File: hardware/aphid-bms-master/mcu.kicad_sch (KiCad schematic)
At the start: 7 parts, among them J6 DEBUG, U1 STM32G491CCTx, Y1 8 MHz

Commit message: Assigned some footprints
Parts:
- C2, C3: footprint (none) -> Capacitor_SMD:C_0805_2012Metric
- J6: footprint (none) -> Connector_PinHeader_1.27mm:PinHeader_2x07_P1.27mm_Vertical_SMD
- JP1: footprint (none) -> Jumper:SolderJumper-2_P1.3mm_Open_TrianglePad1.0x1.5mm
- R3: footprint (none) -> Resistor_SMD:R_0805_2012Metric
- Y1: footprint (none) -> aphid:ABM3-x.xxxMHZ-D2Y-T
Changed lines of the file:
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@@
 			)
 		)
-		(property "Footprint" ""
+		(property "Footprint" "aphid:ABM3-x.xxxMHZ-D2Y-T"
 			(at 54.61 81.28 0)
 			(effects
@@
 			)
 		)
-		(property "Footprint" ""
+		(property "Footprint" "Capacitor_SMD:C_0805_2012Metric"
 			(at 49.2252 91.44 0)
 			(effects
@@
 			)
 		)
-		(property "Footprint" ""
+		(property "Footprint" "Connector_PinHeader_1.27mm:PinHeader_2x07_P1.27mm_Vertical_SMD"
 			(at 45.72 167.64 0)
 			(effects
@@
 			)
 		)
-		(property "Footprint" ""
+		(property "Footprint" "Capacitor_SMD:C_0805_2012Metric"
 			(at 59.9948 91.44 0)
 			(effects
@@
 			)
 		)
-		(property "Footprint" ""
+		(property "Footprint" "Jumper:SolderJumper-2_P1.3mm_Open_TrianglePad1.0x1.5mm"
 			(at 41.91 68.58 0)
 			(effects
@@
 			)
 		)
-		(property "Footprint" ""
+		(property "Footprint" "Resistor_SMD:R_0805_2012Metric"
 			(at 35.052 109.22 90)
 			(effects

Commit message: Worked on BMS master
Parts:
- removed JP1: PRIMARY, Jumper:SolderJumper-2_P1.3mm_Open_TrianglePad1.0x1.5mm, symbol Jumper:SolderJumper_2_Open
- added C16: 100nF, Capacitor_SMD:C_0805_2012Metric, symbol Device:C
- added C17: 1uF, Capacitor_SMD:C_0805_2012Metric, symbol Device:C
- added C18, C19, C20, C21: 100nF, Capacitor_SMD:C_0603_1608Metric, symbol Device:C
- added D5: STATUS, LED_SMD:LED_0805_2012Metric, symbol Device:LED
- added FB1: 600 ohm, Inductor_SMD:L_0805_2012Metric, symbol Device:FerriteBead
- added JP3: BOOT, Jumper:SolderJumper-3_P1.3mm_Bridged12_RoundedPad1.0x1.5mm_NumberLabels, symbol Jumper:SolderJumper_3_Bridged12
- added R12: R, Resistor_SMD:R_0805_2012Metric, symbol Device:R
- C2, C3: value C -> 22pF
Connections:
- net +3.3V: now also J6.3 (VCC), R3.1, U1.1 (VBAT), U1.24 (VDD), U1.36 (VDD), U1.48 (VDD), C19.1, C20.1, C21.1, FB1.1, JP3.3 (B)
- net BOOT1: now also JP3.2 (C)
- net DBG_RX: now also J6.13 (VCP_RX)
- net DBG_TX: now also J6.14 (VCP_TX)
- net DRIVER_FAULT: now also U1.12 (PA4)
- net ENABLE_DRIVER: now also U1.10 (PA2)
- net GND: now also C2.2, C3.2, J6.11 (GNDDetect), J6.5 (GND), J6.7 (GND), U1.19 (VSSA), U1.23 (VSS), U1.35 (VSS), U1.47 (VSS), C16.2, C17.2, C18.2, C19.2, C20.2, C21.2, D5.1 (K), JP3.1 (A)
- net LED: now also R12.1
- net NRST: now also J6.12 (~{RST}), R3.2, C16.1
- net OSC_IN: now also C2.1, Y1.1
- net OSC_OUT: now also C3.1, Y1.2
- net PRIMARY: now also U1.17 (PB1); no longer U1.11 (PA3)
- net RESET_DRIVER: now also U1.11 (PA3)
- net SWCLK: now also J6.6 (JCLK/SWCLK)
- net SWDIO: now also J6.4 (JTMS/SWDIO)
- net SWO: now also J6.8 (JTDO/SWO)
- net VDDA: now reaches U1.20 (VREF+)
- net VDDA: now also U1.21 (VDDA), C17.1, C18.1, FB1.2
- new net: D5.2 (A), R12.2
- no-connect marks 0 -> 14
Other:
- note added: "BOOT0 = Low -> Boot from FLASH BOOT0 = High -> Boot from System memory (ROM bootloader)"
- note added: "CL = 18 pF Cs = ~7 pF CL1 = CL2 = 2 * (Cl - Cs) CL1 = CL2 = 22 pF"
- note added: "Filter Analog supply some extra from noise"
- note added: "One 100 nF decoupling per VDD-pin. Bulk decoupling on Power-sheet"
- note added: "Pull up and filter on NRST to reduce risk of spurious resets"
- company: (none) -> https://aphid-ev.se
- title: (none) -> Aphid BMS Master
- moved on the sheet: C2, C3, R3, Y1

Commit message: Worked on BMS master layout
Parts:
- C2, C3: footprint Capacitor_SMD:C_0805_2012Metric -> Capacitor_SMD:C_0603_1608Metric
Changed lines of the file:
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@@
 			)
 		)
-		(property "Footprint" "Capacitor_SMD:C_0805_2012Metric"
+		(property "Footprint" "Capacitor_SMD:C_0603_1608Metric"
 			(at 33.9852 78.74 0)
 			(effects
@@
 			)
 		)
-		(property "Footprint" "Capacitor_SMD:C_0805_2012Metric"
+		(property "Footprint" "Capacitor_SMD:C_0603_1608Metric"
 			(at 44.7548 78.74 0)
 			(effects

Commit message: Worked on BMS master layout
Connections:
- net CAN1_RX: now also U1.26 (PB12); no longer U1.33 (PA11)
- net CAN1_STB: now also U1.28 (PB14); no longer U1.32 (PA10)
- net CAN1_TX: now also U1.27 (PB13); no longer U1.34 (PA12)
- net CAN2_RX: now also U1.33 (PA11); no longer U1.26 (PB12)
- net CAN2_STB: now also U1.32 (PA10); no longer U1.25 (PB11)
- net CAN2_TX: now also U1.34 (PA12); no longer U1.27 (PB13)
- net LED: now also U1.3 (PC14); no longer U1.16 (PB0)
- net PRIMARY: now also U1.30 (PA8); no longer U1.17 (PB1)
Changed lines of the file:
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@@
 		(color 0 0 0 0)
 	)
-	(no_connect
-		(at 121.92 123.19)
+	(junction
+		(at 154.94 80.01)
+		(diameter 0)
+		(color 0 0 0 0)
+	)
+	(no_connect
+		(at 121.92 115.57)
 	)
 	(no_connect
@@
 	)
 	(no_connect
+		(at 121.92 90.17)
+	)
+	(no_connect
 		(at 121.92 82.55)
 	)
@@
 	)
 	(no_connect
-		(at 121.92 80.01)
-	)
-	(no_connect
-		(at 154.94 80.01)
+		(at 121.92 87.63)
 	)
 	(wire
@@
 	(wire
 		(pts
-			(xy 109.22 115.57) (xy 121.92 115.57)
+			(xy 110.49 123.19) (xy 121.92 123.19)
 		)
 		(stroke
@@
 	(wire
 		(pts
-			(xy 109.22 90.17) (xy 121.92 90.17)
+			(xy 166.37 80.01) (xy 154.94 80.01)
 		)
 		(stroke
@@
 	(wire
 		(pts
-			(xy 109.22 120.65) (xy 121.92 120.65)
+			(xy 110.49 120.65) (xy 121.92 120.65)
 		)
 		(stroke
@@
 	(wire
 		(pts
-			(xy 109.22 118.11) (xy 121.92 118.11)
+			(xy 110.49 118.11) (xy 121.92 118.11)
 		)
 		(stroke
@@
 	(wire
 		(pts
-			(xy 109.22 125.73) (xy 121.92 125.73)
+			(xy 110.49 125.73) (xy 121.92 125.73)
 		)
 		(stroke
@@
 	(wire
 		(pts
-			(xy 113.03 87.63) (xy 121.92 87.63)
+			(xy 113.03 80.01) (xy 121.92 80.01)
 		)
 		(stroke
@@
 		(pts
 			(xy 250.19 85.09) (xy 250.19 87.63)
+		)
+		(stroke
+			(width 0)
+			(type default)
+		)
+	)
+	(wire
+		(pts
+			(xy 153.67 80.01) (xy 154.94 80.01)
 		)
 		(stroke
@@
 	)
 	(label "LED"
-		(at 113.03 87.63 0)
+		(at 113.03 80.01 0)
 		(fields_autoplaced yes)
 		(effects
@@
 	(hierarchical_label "CAN2_RX"
 		(shape input)
-		(at 109.22 118.11 180)
-		(fields_autoplaced yes)
-		(effects
-			(font
-				(size 1.27 1.27)
-			)
-			(justify right)
+		(at 166.37 87.63 0)
+		(fields_autoplaced yes)
+		(effects
+			(font
+				(size 1.27 1.27)
+			)
+			(justify left)
 		)
 	)
 	(hierarchical_label "CAN1_STB"
 		(shape output)
-		(at 166.37 85.09 0)
-		(fields_autoplaced yes)
-		(effects
-			(font
-				(size 1.27 1.27)
-			)
-			(justify left)
+		(at 110.49 123.19 180)
+		(fields_autoplaced yes)
+		(effects
+			(font
+				(size 1.27 1.27)
+			)
+			(justify right)
 		)
 	)
 	(hierarchical_label "CAN2_TX"
 		(shape output)
-		(at 109.22 120.65 180)
-		(fields_autoplaced yes)
-		(effects
-			(font
-				(size 1.27 1.27)
-			)
-			(justify right)
+		(at 166.37 90.17 0)
+		(fields_autoplaced yes)
+		(effects
+			(font
+				(size 1.27 1.27)
+			)
+			(justify left)
 		)
 	)
@@
 	(hierarchical_label "PRIMARY"
 		(shape input)
-		(at 109.22 90.17 180)
-		(fields_autoplaced yes)
-		(effects
-			(font
-				(size 1.27 1.27)
-			)
-			(justify right)
+		(at 166.37 80.01 0)
+		(fields_autoplaced yes)
+		(effects
+			(font
+				(size 1.27 1.27)
+			)
+			(justify left)
 		)
 	)
@@
 	(hierarchical_label "CAN1_RX"
 		(shape input)
-		(at 166.37 87.63 0)
-		(fields_autoplaced yes)
-		(effects
-			(font
-				(size 1.27 1.27)
-			)
-			(justify left)
+		(at 110.49 118.11 180)
+		(fields_autoplaced yes)
+		(effects
+			(font
+				(size 1.27 1.27)
+			)
+			(justify right)
 		)
 	)
@@
 	(hierarchical_label "CAN2_STB"
 		(shape output)
-		(at 109.22 115.57 180)
-		(fields_autoplaced yes)
-		(effects
-			(font
-				(size 1.27 1.27)
-			)
-			(justify right)
+		(at 166.37 85.09 0)
+		(fields_autoplaced yes)
+		(effects
+			(font
+				(size 1.27 1.27)
+			)
+			(justify left)
 		)
 	)
 	(hierarchical_label "ENABLE_SLAVES"
 		(shape output)
-		(at 109.22 125.73 180)
+		(at 110.49 125.73 180)
 		(fields_autoplaced yes)
 		(effects
@@
 	(hierarchical_label "CAN1_TX"
 		(shape output)
-		(at 166.37 90.17 0)
-		(fields_autoplaced yes)
-		(effects
-			(font
-				(size 1.27 1.27)
-			)
-			(justify left)
-		)
-	)
+		(at 110.49 120.65 180)
+		(fields_autoplaced yes)
+		(effects
+			(font
+				(size 1.27 1.27)
+			)
+			(justify right)
+		)
+	)

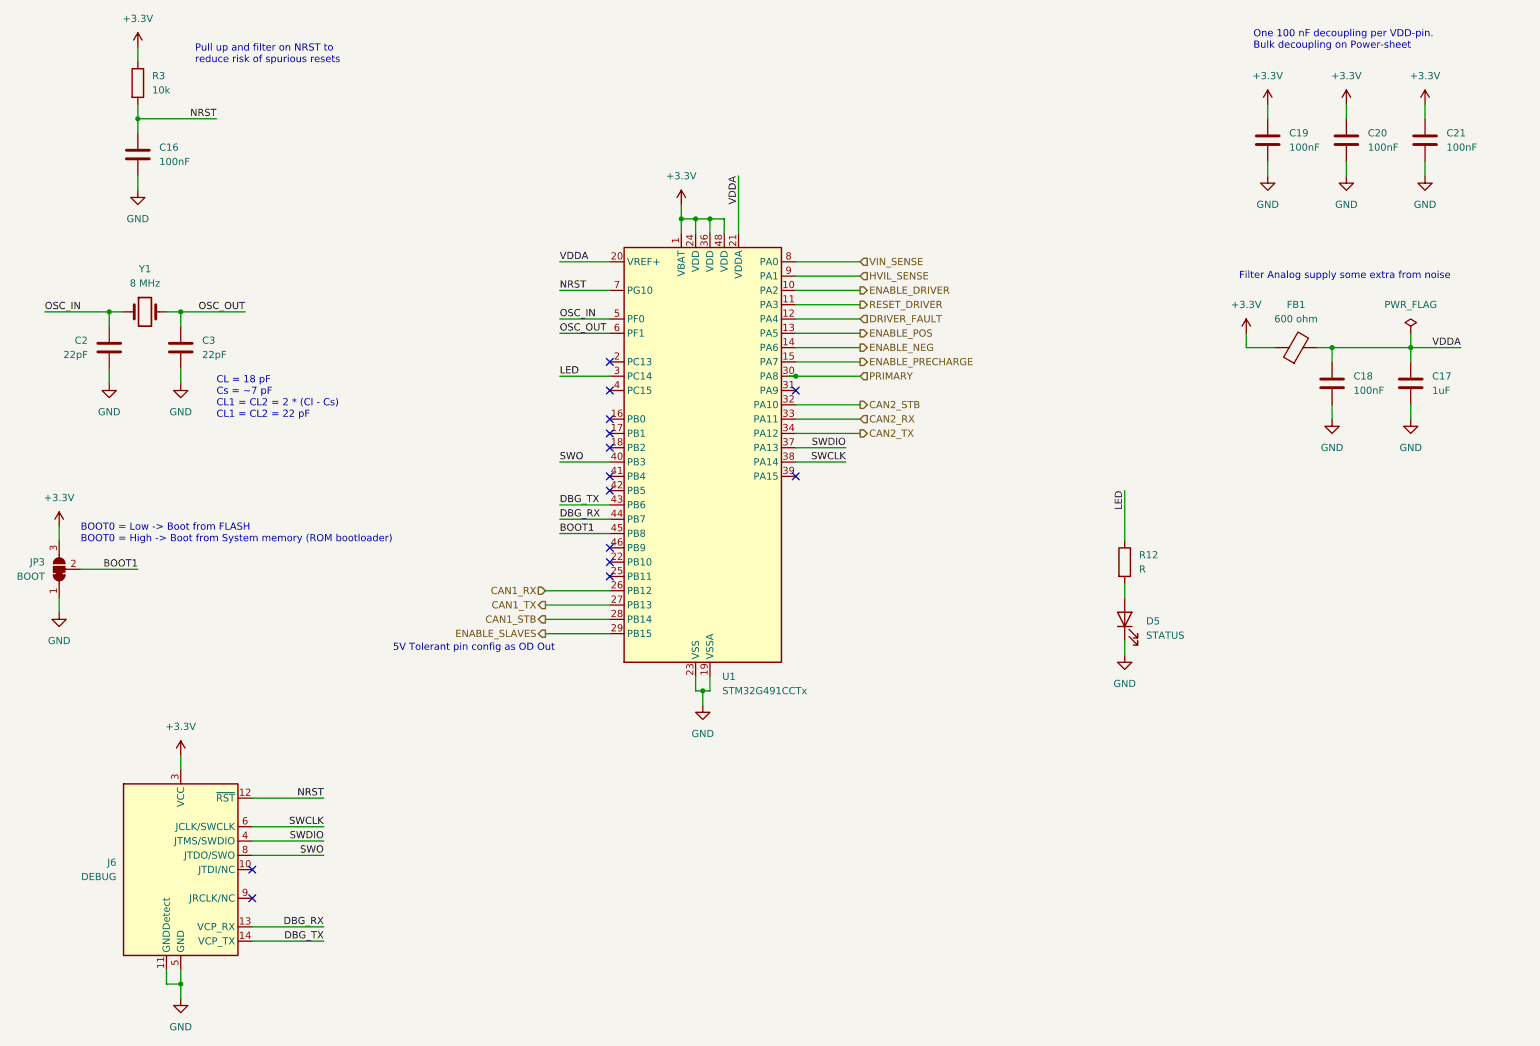
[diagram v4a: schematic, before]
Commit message: Changed BMS Master to use MAX17851 instead of isolated CAN
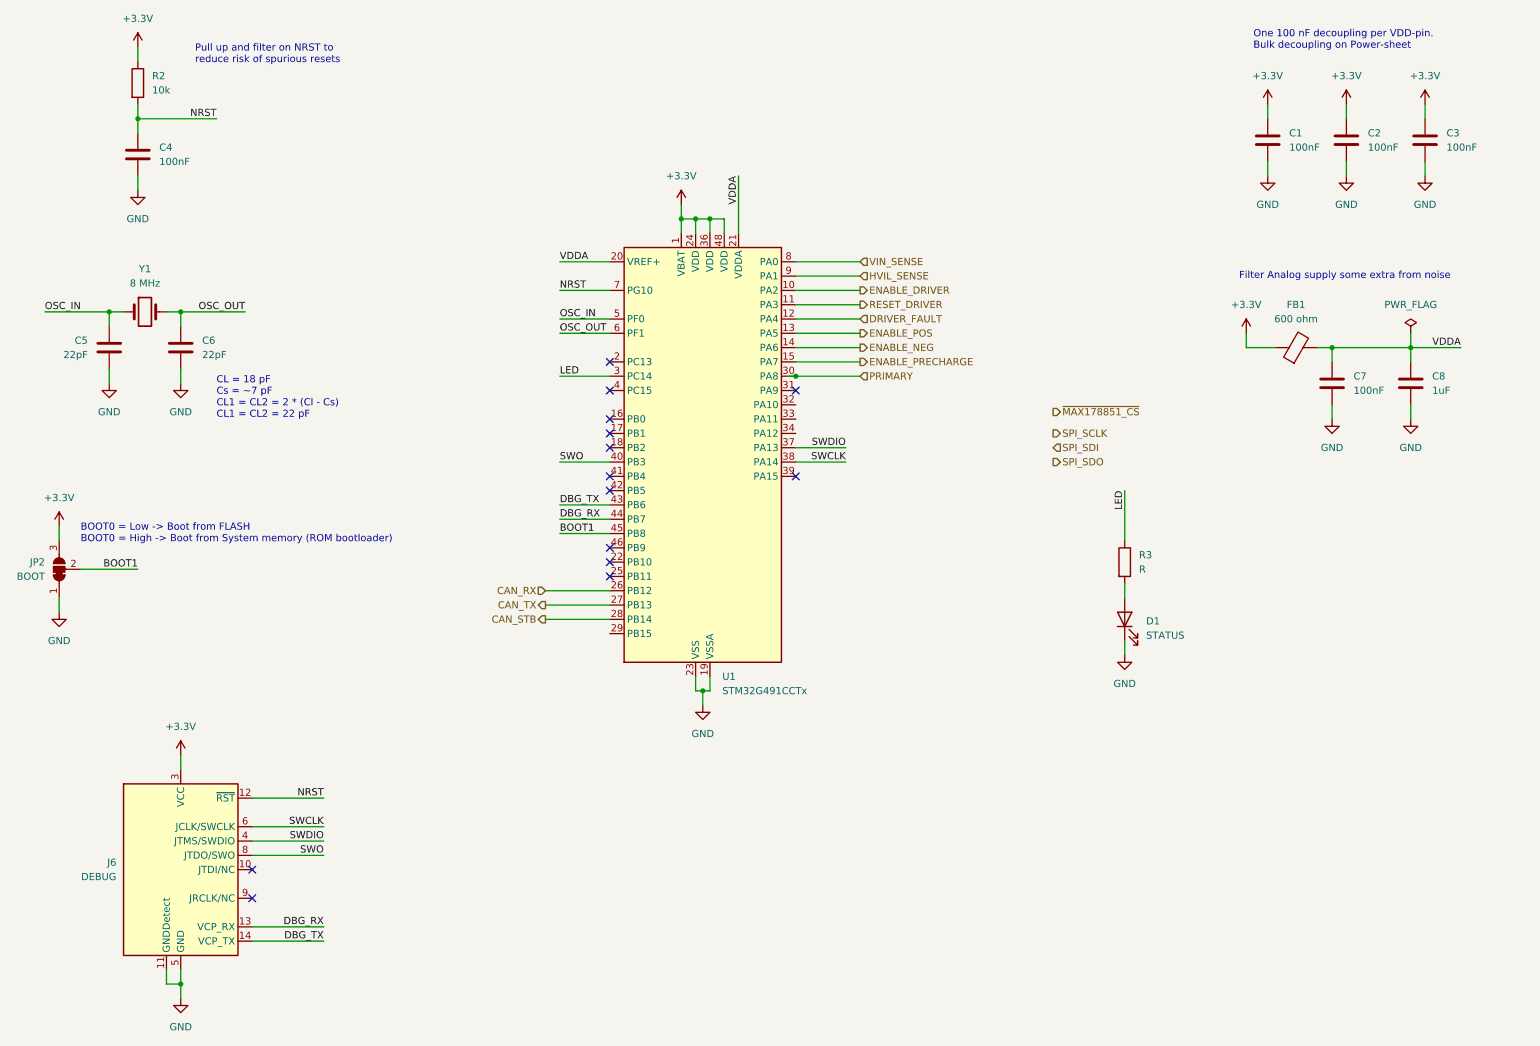
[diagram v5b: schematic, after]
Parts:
- renumbered C19 to C1, C20 to C2, C21 to C3, C16 to C4, C2 to C5, C3 to C6, C18 to C7, C17 to C8, D5 to D1, JP3 to JP2, R3 to R2, R12 to R3
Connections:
- net CAN1_RX renamed CAN_RX
- net CAN1_STB renamed CAN_STB
- net CAN1_TX renamed CAN_TX
- net CAN2_RX: no longer names the net of U1.33 (PA11)
- net CAN2_STB: no longer names the net of U1.32 (PA10)
- net CAN2_TX: no longer names the net of U1.34 (PA12)
- net ENABLE_SLAVES: no longer names the net of U1.29 (PB15)
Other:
- note removed: "5V Tolerant pin config as OD Out"

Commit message: Harmonized VC and BMS components
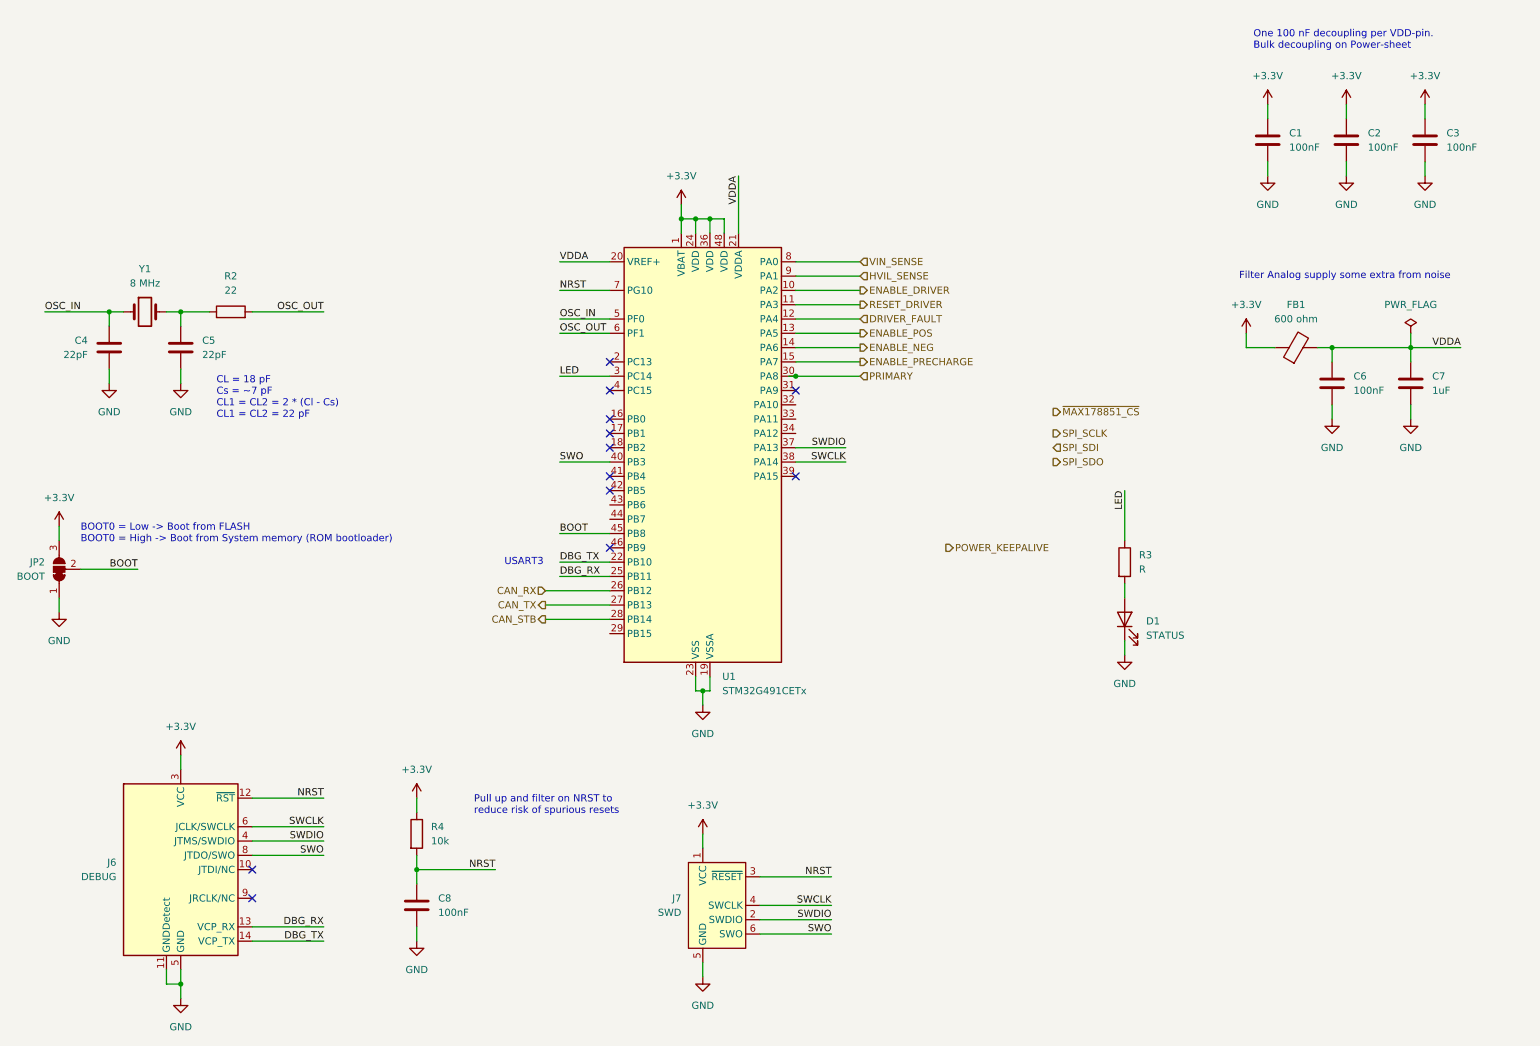
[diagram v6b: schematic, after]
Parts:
- removed U1: STM32G491CCTx, Package_QFP:LQFP-48_7x7mm_P0.5mm, symbol MCU_ST_STM32G4:STM32G491CCTx
- added J7: SWD, Connector:Tag-Connect_TC2030-IDC-FP_2x03_P1.27mm_Vertical, symbol Connector:Conn_ARM_SWD_TagConnect_TC2030
- added R2: 22, Resistor_SMD:R_0805_2012Metric, symbol Device:R
- added U1: STM32G491CETx, Package_QFP:LQFP-48_7x7mm_P0.5mm, symbol MCU_ST_STM32G4:STM32G491CETx
- renumbered C5 to C4, C6 to C5, C7 to C6, C8 to C7, C4 to C8, R2 to R4
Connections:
- net +3.3V: now also J7.1 (VCC), U1.1 (VBAT), U1.24 (VDD), U1.36 (VDD), U1.48 (VDD)
- net CAN_RX: now also U1.26 (PB12)
- net CAN_STB: now also U1.28 (PB14)
- net CAN_TX: now also U1.27 (PB13)
- net DBG_RX: now also U1.25 (PB11)
- net DBG_TX: now also U1.22 (PB10)
- net DRIVER_FAULT: now also U1.12 (PA4)
- net ENABLE_DRIVER: now also U1.10 (PA2)
- net ENABLE_NEG: now also U1.14 (PA6)
- net ENABLE_POS: now also U1.13 (PA5)
- net ENABLE_PRECHARGE: now also U1.15 (PA7)
- net GND: now also J7.5 (GND), U1.19 (VSSA), U1.23 (VSS), U1.35 (VSS), U1.47 (VSS)
- net HVIL_SENSE: now also U1.9 (PA1)
- net LED: now also U1.3 (PC14)
- net NRST: now also J7.3 (~{RESET}), U1.7 (PG10)
- net OSC_IN: now also U1.5 (PF0)
- net OSC_OUT: now also R2.2, U1.6 (PF1); no longer C5.1, Y1.2
- net PRIMARY: now also U1.30 (PA8)
- net RESET_DRIVER: now also U1.11 (PA3)
- net SWCLK: now also J7.4 (SWCLK), U1.38 (PA14)
- net SWDIO: now also J7.2 (SWDIO), U1.37 (PA13)
- net SWO: now also J7.6 (SWO), U1.40 (PB3)
- net VDDA: now also U1.20 (VREF+), U1.21 (VDDA)
- net VIN_SENSE: now also U1.8 (PA0)
- net BOOT1 renamed BOOT
- net BOOT: now also U1.45 (PB8)
- new net: C5.1, R2.1, Y1.2
- no-connect marks 14 -> 12
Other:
- note added: "USART3"
- moved on the sheet: C8, R4
